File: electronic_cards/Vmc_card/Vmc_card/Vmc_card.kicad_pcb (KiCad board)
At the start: 2 copper layers, 31 x 18 mm, 3 parts, among them J1 Input, J2 Servo_flap, J3 Fan

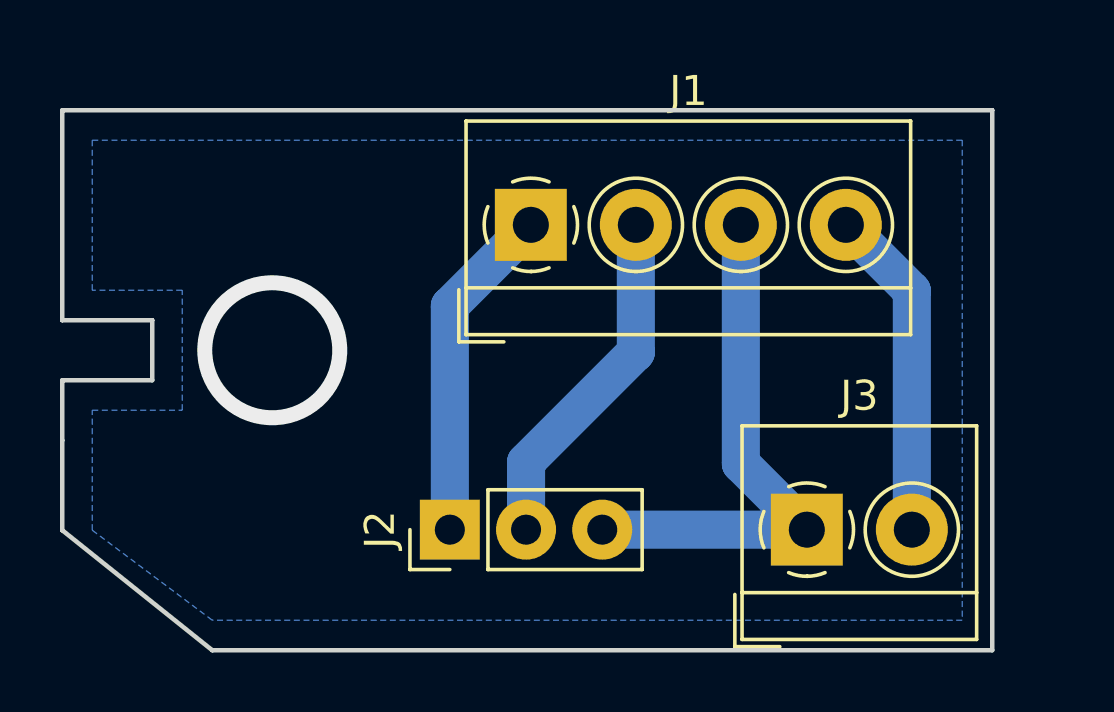
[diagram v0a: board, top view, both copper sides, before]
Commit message: Add Vmc control and remove any bugs
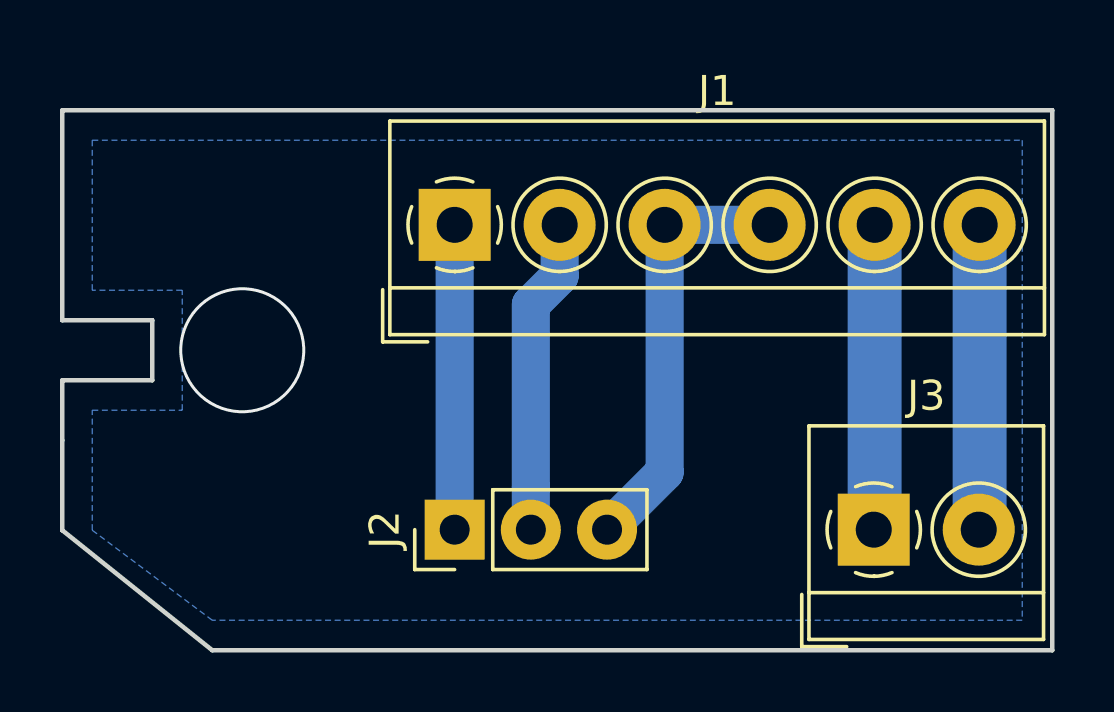
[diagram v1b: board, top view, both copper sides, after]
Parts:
- J1: footprint TerminalBlock_4Ucon:TerminalBlock_4Ucon_1x04_P3.50mm_Horizontal -> TerminalBlock_4Ucon:TerminalBlock_4Ucon_1x06_P3.50mm_Horizontal
- moved J1 2.54 mm to (132.1, 83.8)
- moved J3 2.23 mm to (146.1, 94.0)
- moved J2 0.16 mm to (132.1, 94.0)
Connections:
- net +5V renamed Net-(J1-Pad2)
- J1 pad 4: +24V -> GND
- J3 pad 1: GND -> Net-(J1-Pad5)
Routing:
- net Net-(J1-Pad5): track 0.00 -> 10.2 mm
- net GND: track 17.9 -> 14.5 mm
- net Net-(J1-Pad1): track 11.3 -> 10.2 mm
- net Net-(J1-Pad2): track 11.7 -> 10.6 mm
- net +24V: track 11.1 -> 10.2 mm
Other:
- board size 31 x 18 mm -> 33 x 18 mm
